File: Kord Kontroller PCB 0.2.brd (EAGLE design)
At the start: 242.5 x 100 mm, 190 parts, among them IC2 74HCT1G125DBV, J1 MIDIOUTB, J2 MIDIOUTA, J3 FTSH-105-01-L-DV-KJ, Q1 32kHz, SW2 SPST_TACT-KMR2, U1 AP2112K-3.3, U2 ATSAMD51J19A-AUT

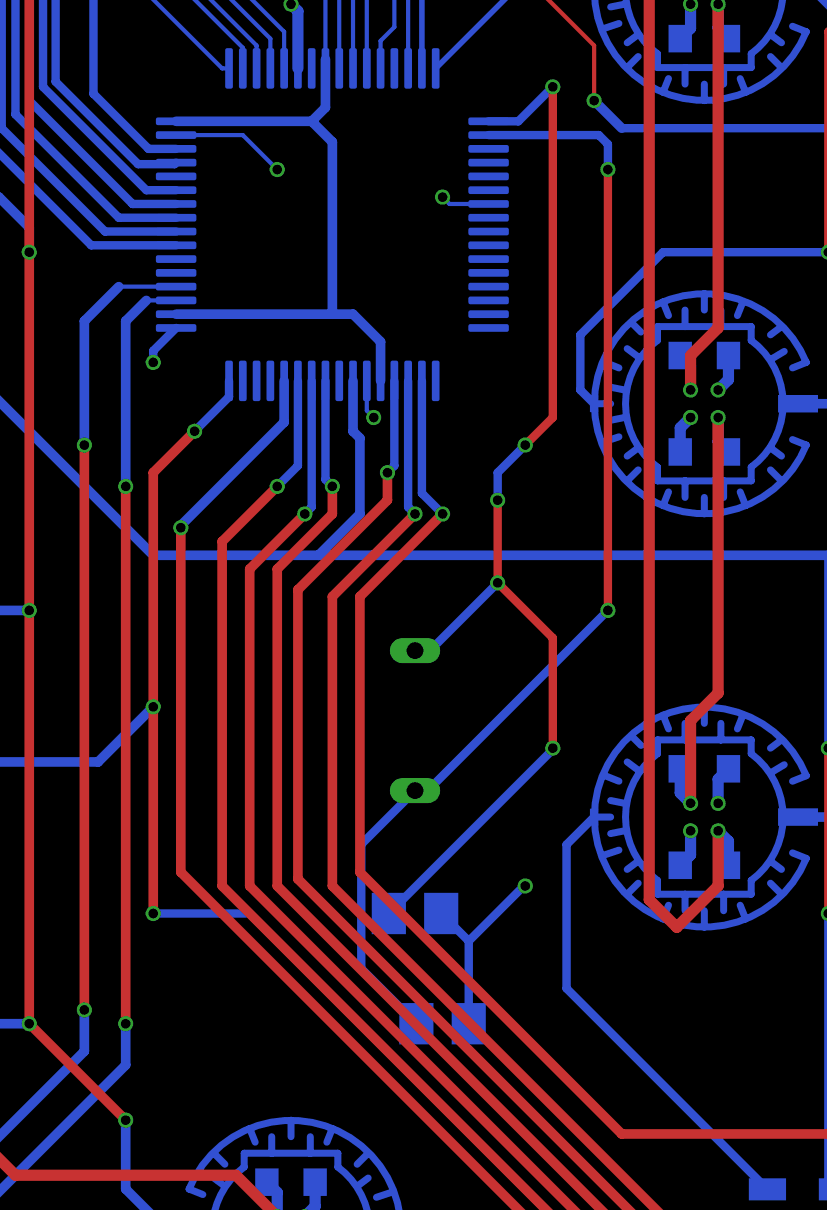
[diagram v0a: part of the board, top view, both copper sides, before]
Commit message: changed crystal
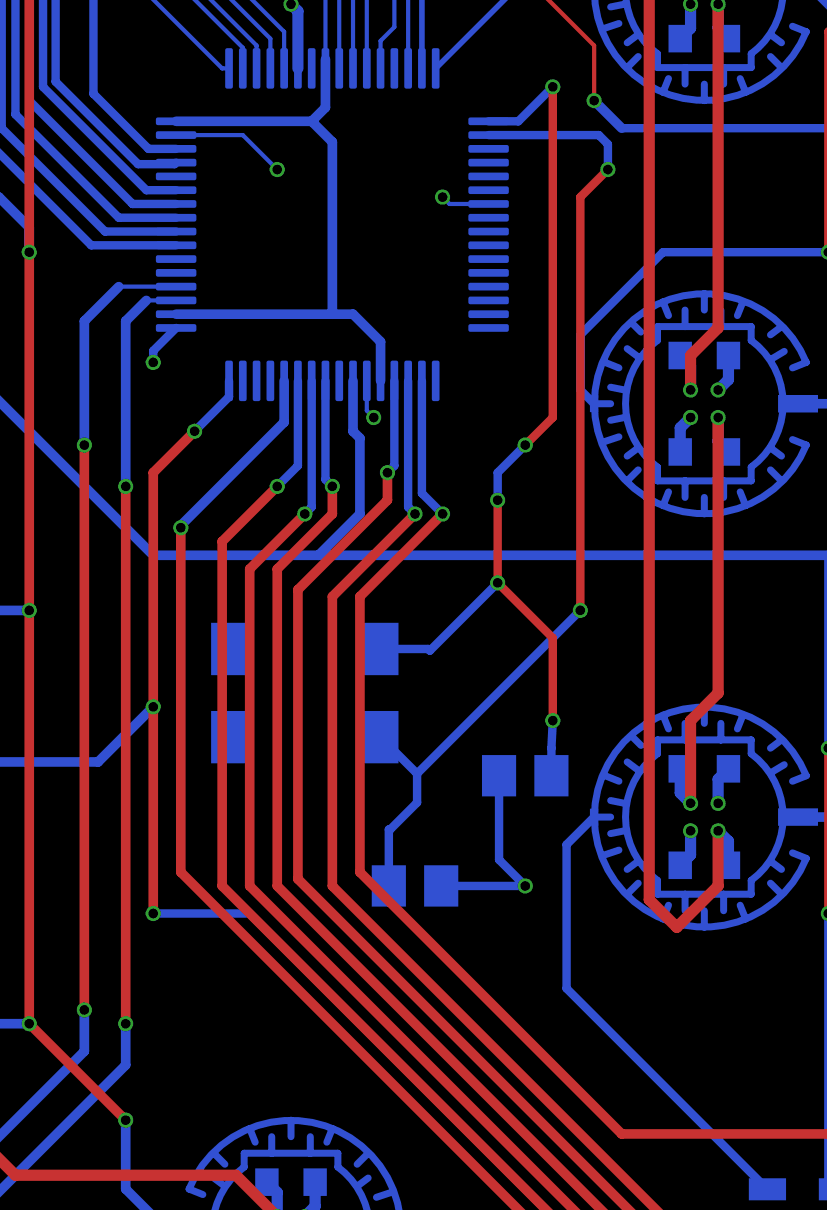
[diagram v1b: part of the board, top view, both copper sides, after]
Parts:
- removed Q1: 32kHz, special:QS
- added Y1: ECS-.327-12.5-17X-TR, ECS-.327-12.5-17X-TR:XTAL_ECS-.327-12.5-17X-TR
- moved C8 6.40 mm to (136.0, 24.0), turned to 0 degrees
- moved C7 5.10 mm to (132.0, 20.0)
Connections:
- net OSCIN: now also Y1.4; no longer Q1.1
- net OSCOUT: now also Y1.1; no longer Q1.2
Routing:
- net OSCIN: track 41.0 -> 34.8 mm
- net OSCOUT: track 41.2 -> 36.6 mm
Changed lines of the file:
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@@
 </element>
 <element name="B29" library="microbuilder" package="ELAST_PAD_SQUARE_10MM_4X4WIDE" value="ELAST_10X10" x="127.5" y="7.5" smashed="yes" rot="MR180"/>
-<element name="C7" library="microbuilder" package="0805-NO" value="10uF" x="133" y="15" smashed="yes" rot="MR180">
-<attribute name="NAME" x="135.032" y="15.127" size="0.8128" layer="26" ratio="18" rot="MR180"/>
-<attribute name="VALUE" x="135.032" y="15.762" size="0.4064" layer="28" ratio="10" rot="MR180"/>
+<element name="C7" library="microbuilder" package="0805-NO" value="10uF" x="132" y="20" smashed="yes" rot="MR180">
+<attribute name="NAME" x="134.032" y="20.127" size="0.8128" layer="26" ratio="18" rot="MR180"/>
+<attribute name="VALUE" x="134.032" y="20.762" size="0.4064" layer="28" ratio="10" rot="MR180"/>
 </element>
-<element name="C8" library="microbuilder" package="0805-NO" value="10uF" x="132" y="19" smashed="yes" rot="MR180">
-<attribute name="NAME" x="134.032" y="19.127" size="0.8128" layer="26" ratio="18" rot="MR180"/>
-<attribute name="VALUE" x="134.032" y="19.762" size="0.4064" layer="28" ratio="10" rot="MR180"/>
-</element>
-<element name="Q1" library="special" library_urn="urn:adsk.eagle:library:367" package="QS" package3d_urn="urn:adsk.eagle:package:26647/2" value="32kHz" x="132" y="26" smashed="yes" rot="MR270">
-<attribute name="NAME" x="129.333" y="31.08" size="1.27" layer="26" ratio="10" rot="MR270"/>
-<attribute name="VALUE" x="135.937" y="31.08" size="1.27" layer="28" ratio="10" rot="MR270"/>
+<element name="C8" library="microbuilder" package="0805-NO" value="10uF" x="136" y="24" smashed="yes" rot="MR0">
+<attribute name="NAME" x="133.968" y="23.873" size="0.8128" layer="26" ratio="18" rot="MR0"/>
+<attribute name="VALUE" x="133.968" y="23.238" size="0.4064" layer="28" ratio="10" rot="MR0"/>
 </element>
 <element name="J4" library="SparkFun-Connectors" package="USB-MICROB-PTH-MILL" value="" x="127.1" y="94.9" smashed="yes" rot="MR180">
@@
 <attribute name="VALUE" x="125.83" y="100.361" size="0.508" layer="28" font="vector" rot="MR180"/>
 </element>
+<element name="Y1" library="ECS-.327-12.5-17X-TR" package="XTAL_ECS-.327-12.5-17X-TR" value="ECS-.327-12.5-17X-TR" x="128" y="27" smashed="yes" rot="MR0">
+<attribute name="DESCRIPTION" value=" 32.768kHz ±20ppm Crystal 12.5pF 50 kOhms 4-SOJ, 5.50mm pitch " x="128" y="27" size="1.778" layer="28" rot="MR0" display="off"/>
+<attribute name="DIGI-KEY_PART_NUMBER" value="XC1195CT-ND" x="128" y="27" size="1.778" layer="28" rot="MR0" display="off"/>
+<attribute name="DIGI-KEY_PURCHASE_URL" value="https://www.digikey.com/product-detail/en/ecs-inc/ECS-.327-12.5-17X-TR/XC1195CT-ND/827659?utm_source=snapeda&amp;utm_medium=aggregator&amp;utm_campaign=symbol" x="128" y="27" size="1.778" layer="28" rot="MR0" display="off"/>
+<attribute name="MF" value="ECS Inc." x="128" y="27" size="1.778" layer="28" rot="MR0" display="off"/>
+<attribute name="MP" value="ECS-.327-12.5-17X-TR" x="128" y="27" size="1.778" layer="28" rot="MR0" display="off"/>
+<attribute name="NAME" x="131.64103125" y="30.000609375" size="0.751659375" layer="26" rot="MR0"/>
+<attribute name="PACKAGE" value="4-4 ECS International" x="128" y="27" size="1.778" layer="28" rot="MR0" display="off"/>
+<attribute name="VALUE" x="131.6373" y="23.3707" size="0.7508875" layer="28" rot="MR0"/>
+</element>
 </elements>
 <signals>
@@
 <contactref element="C7" pad="2"/>
 <contactref element="C8" pad="2"/>
-<wire x1="136" y1="20" x2="135.95" y2="20" width="0.3048" layer="16"/>
-<wire x1="135.95" y1="20" x2="133.95" y2="18" width="0.3048" layer="16"/>
-<wire x1="133.95" y1="15" x2="133.95" y2="18" width="0.3048" layer="16"/>
+<wire x1="136" y1="20" x2="132.95" y2="20" width="0.3048" layer="16"/>
 <via x="136" y="20" extent="1-16" drill="0.35"/>
-<wire x1="132.95" y1="19" x2="133.95" y2="18" width="0.3048" layer="16"/>
 <wire x1="123.33" y1="47.25" x2="125.75" y2="47.25" width="0.1524" layer="16"/>
 <wire x1="125.75" y1="47.25" x2="127" y2="46" width="0.1524" layer="16"/>
@@
 <wire x1="129.82858125" y1="97.43091875" x2="131.202465625" y2="98" width="0.4064" layer="1" curve="-45"/>
 <wire x1="131.202465625" y1="98" x2="132" y2="98" width="0.4064" layer="1"/>
+<wire x1="135.05" y1="24" x2="135.05" y2="20.95" width="0.3048" layer="16"/>
+<wire x1="135.05" y1="20.95" x2="136" y2="20" width="0.3048" layer="16"/>
 </signal>
 <signal name="ROW1">
@@
 </signal>
 <signal name="OSCIN">
-<contactref element="U2" pad="1"/>
-<contactref element="Q1" pad="1"/>
 <contactref element="C8" pad="1"/>
-<wire x1="134.67" y1="47.75" x2="135.75" y2="47.75" width="0.3048" layer="16"/>
-<wire x1="135.75" y1="47.75" x2="137" y2="49" width="0.3048" layer="16"/>
 <via x="137" y="49" extent="1-16" drill="0.35"/>
+<wire x1="135.75" y1="47.75" x2="137" y2="49" width="0.3048" layer="16"/>
 <wire x1="137" y1="49" x2="137" y2="37" width="0.3048" layer="1"/>
 <wire x1="137" y1="37" x2="136" y2="36" width="0.3048" layer="1"/>
@@
 <wire x1="135" y1="34" x2="135" y2="31" width="0.3048" layer="1"/>
 <via x="135" y="31" extent="1-16" drill="0.35"/>
-<wire x1="135" y1="31" x2="132.54" y2="28.54" width="0.3048" layer="16"/>
-<wire x1="132.54" y1="28.54" x2="132" y2="28.54" width="0.3048" layer="16"/>
-<wire x1="131.05" y1="19" x2="137" y2="24.95" width="0.3048" layer="16"/>
-<wire x1="137" y1="24.95" x2="137" y2="25" width="0.3048" layer="16"/>
-<via x="137" y="25" extent="1-16" drill="0.35"/>
-<wire x1="137" y1="25" x2="137" y2="29" width="0.3048" layer="1"/>
+<wire x1="132.54" y1="28.54" x2="135" y2="31" width="0.3048" layer="16"/>
+<wire x1="137" y1="26" x2="136.95" y2="25" width="0.3048" layer="16"/>
+<wire x1="136.95" y1="25" x2="136.95" y2="24" width="0.3048" layer="16"/>
+<via x="137" y="26" extent="1-16" drill="0.35"/>
+<wire x1="137" y1="26" x2="137" y2="29" width="0.3048" layer="1"/>
 <wire x1="137" y1="29" x2="135" y2="31" width="0.3048" layer="1"/>
+<contactref element="U2" pad="1"/>
+<contactref element="Y1" pad="4"/>
+<wire x1="130.75" y1="28.6" x2="132.48" y2="28.6" width="0.3048" layer="16"/>
+<wire x1="132.48" y1="28.6" x2="132.54" y2="28.54" width="0.3048" layer="16"/>
+<wire x1="134.67" y1="47.75" x2="135.75" y2="47.75" width="0.3048" layer="16"/>
 </signal>
 <signal name="OSCOUT">
 <contactref element="U2" pad="2"/>
-<contactref element="Q1" pad="2"/>
-<contactref element="C7" pad="1"/>
 <wire x1="138.67" y1="47.25" x2="134.67" y2="47.25" width="0.3048" layer="16"/>
-<wire x1="139" y1="30" x2="132.46" y2="23.46" width="0.3048" layer="16"/>
-<wire x1="132" y1="23.46" x2="132.46" y2="23.46" width="0.3048" layer="16"/>
-<via x="139" y="30" extent="1-16" drill="0.35"/>
-<wire x1="139" y1="30" x2="139" y2="46" width="0.3048" layer="1"/>
+<wire x1="132.075" y1="24.075" x2="138" y2="30" width="0.3048" layer="16"/>
+<via x="138" y="30" extent="1-16" drill="0.35"/>
+<wire x1="138" y1="45" x2="139" y2="46" width="0.3048" layer="1"/>
+<wire x1="138" y1="45" x2="138" y2="30" width="0.3048" layer="1"/>
 <via x="139" y="46" extent="1-16" drill="0.35"/>
 <wire x1="139" y1="46" x2="139" y2="46.92" width="0.3048" layer="16"/>
 <wire x1="139" y1="46.92" x2="138.67" y2="47.25" width="0.3048" layer="16"/>
-<wire x1="132" y1="23.46" x2="130.05" y2="21.51" width="0.3048" layer="16"/>
-<wire x1="130.05" y1="21.51" x2="130.05" y2="17" width="0.3048" layer="16"/>
-<wire x1="130.05" y1="17" x2="132.05" y2="15" width="0.3048" layer="16"/>
+<contactref element="C7" pad="1"/>
+<contactref element="Y1" pad="1"/>
+<wire x1="130.75" y1="25.4" x2="132.075" y2="24.075" width="0.3048" layer="16"/>
+<wire x1="131.05" y1="20" x2="131.05" y2="22.05" width="0.3048" layer="16"/>
+<wire x1="132.075" y1="23.025" x2="132.075" y2="24.075" width="0.3048" layer="16"/>
+<wire x1="131.05" y1="22.05" x2="131.1" y2="22.05" width="0.3048" layer="16"/>
+<wire x1="131.1" y1="22.05" x2="132.075" y2="23.025" width="0.3048" layer="16"/>
 </signal>
 <signal name="VSW">

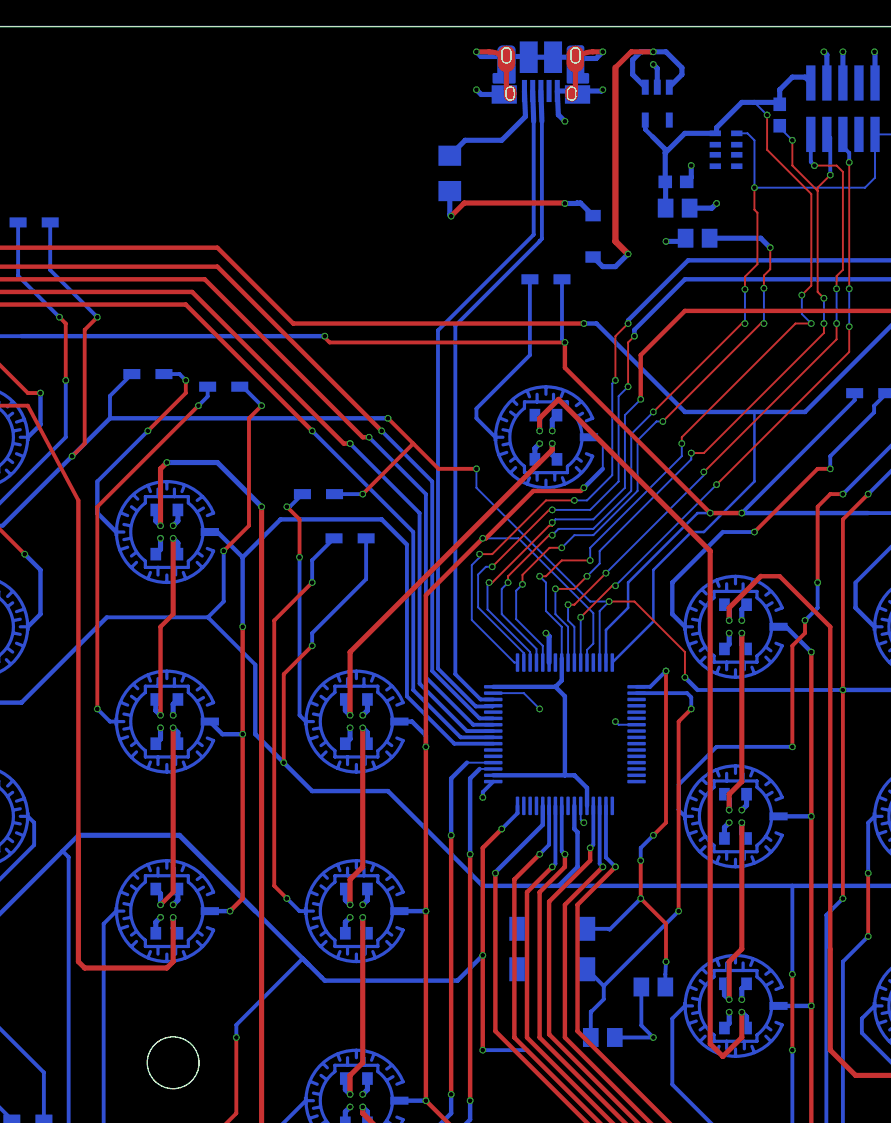
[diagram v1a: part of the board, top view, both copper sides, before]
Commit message: Level shifter and decouplers
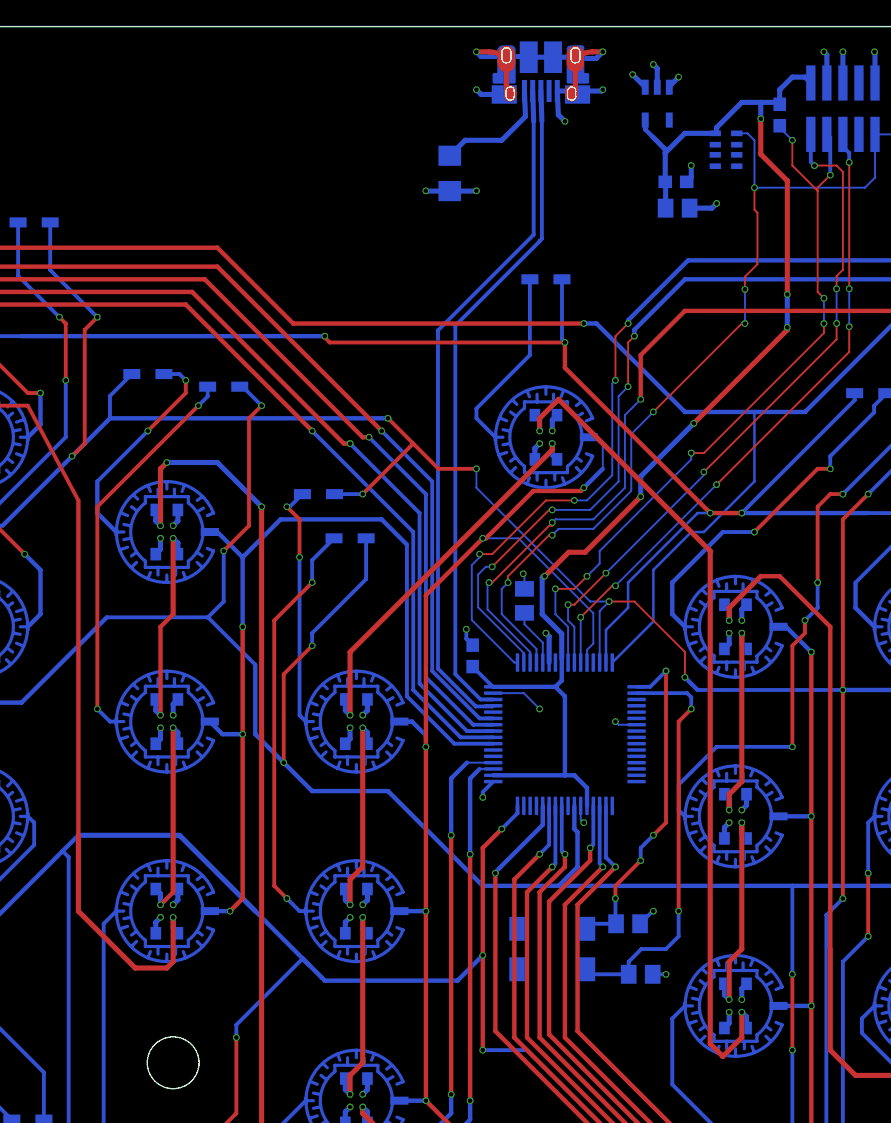
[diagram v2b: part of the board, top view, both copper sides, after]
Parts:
- removed D59: MBR120, adafruit:SOD-123FL
- added C12: 1uF, microbuilder:0603-NO
- moved C1 31.8 mm to (125.8, 54.5), turned to 90 degrees
- moved C7 5.83 mm to (135.0, 25.0)
- moved C8 5.39 mm to (134.0, 29.0), turned to 180 degrees
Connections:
- removed net VBUS: D59.A, PTC1.1
- net 3.3V: now also C12.1
- net GND: now also C12.2
- net VDD: now also PTC1.1; no longer D59.C
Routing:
- net VDDCORE1: track 49.0 -> 4.53 mm, vias 6 -> 0
- net VDD: track 117.5 -> 92.7 mm, vias 62 -> 64
- net VBUS: track 14.1 -> 0.00 mm, vias 2 -> 0
- net OSCIN: track 34.8 -> 27.1 mm, vias 5 -> 4
- net GND: track 156.9 -> 153.0 mm, vias 82 -> 84
- net OSCOUT: track 36.6 -> 33.1 mm
- net N$113: track 65.0 -> 62.6 mm
- net 3.3V: track 105.5 -> 103.7 mm
